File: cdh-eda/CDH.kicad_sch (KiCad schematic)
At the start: 4 parts

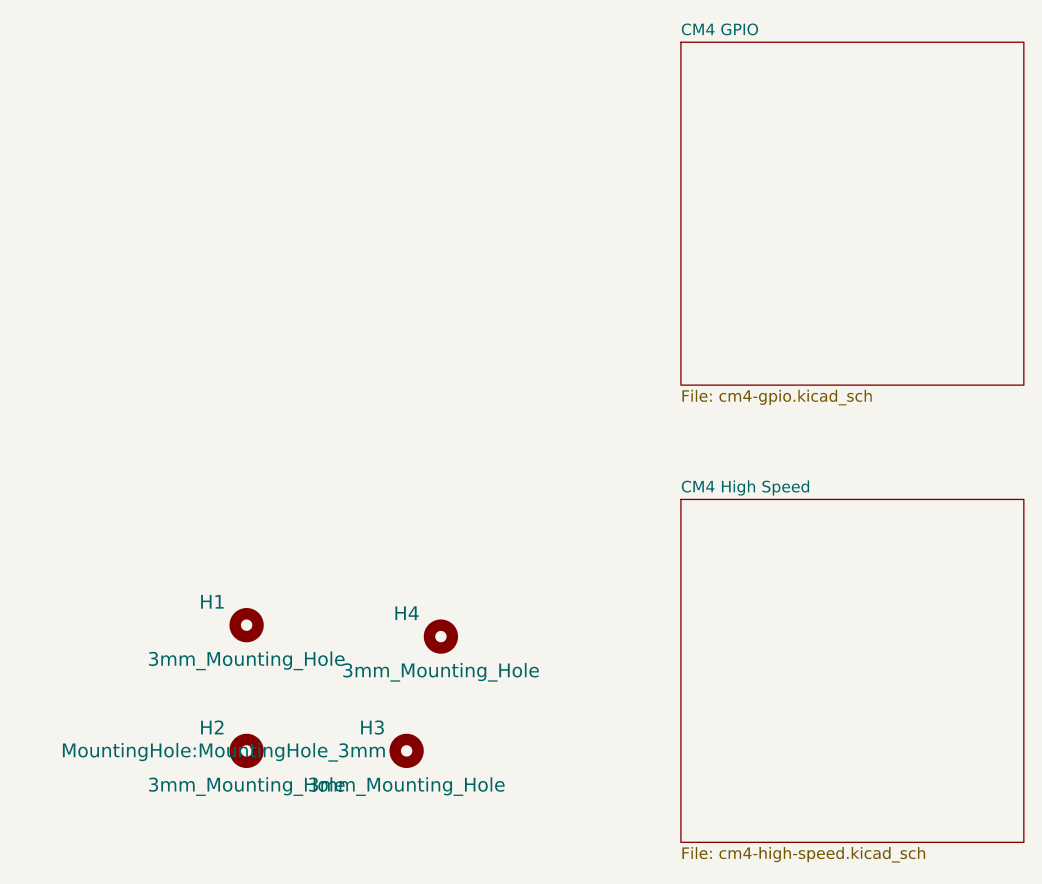
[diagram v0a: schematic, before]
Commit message: V.2 updates
 1. Add jumper CAN resistors
 2. Add camera connector
 3. Add display connector
 5. Updated CAN transceiver protective circuitry
 6. Add MCP2515 interrupt GPIO pin 18
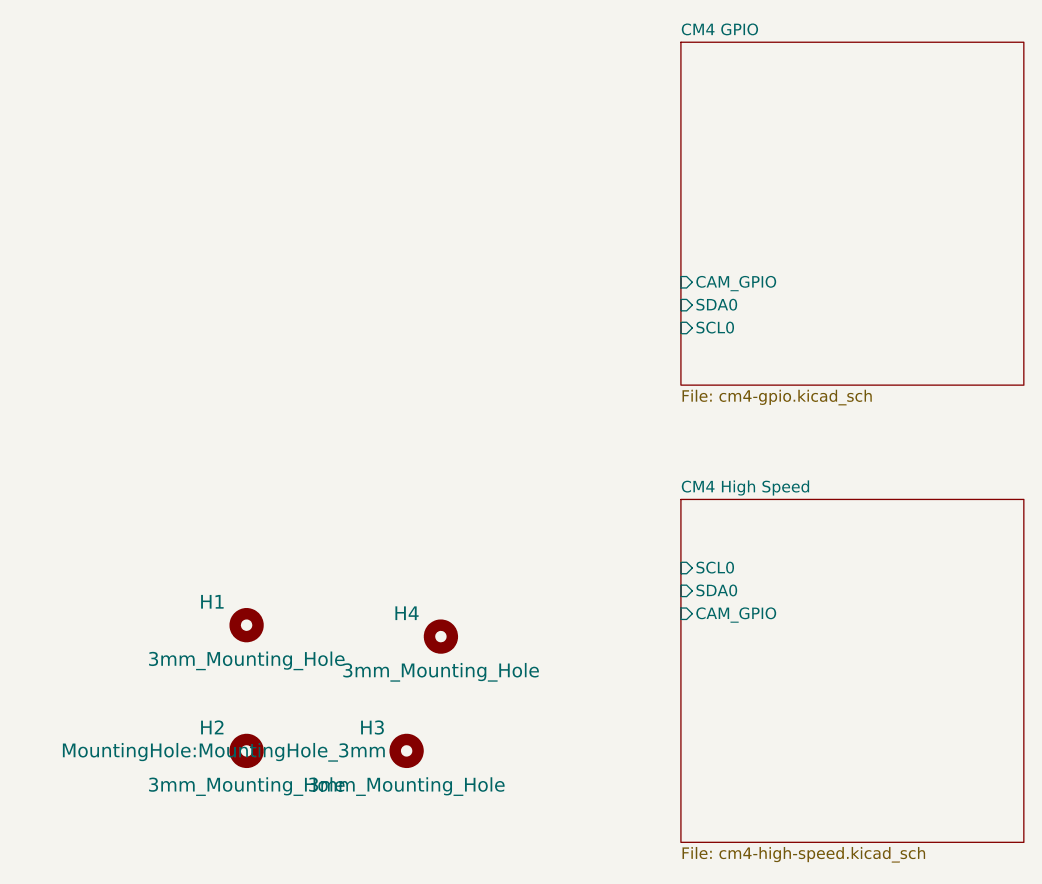
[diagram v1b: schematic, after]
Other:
- sheet CM4 GPIO ports: added CAM_GPIO, SCL0, SDA0; removed none
- sheet CM4 High Speed ports: added CAM_GPIO, SCL0, SDA0; removed none
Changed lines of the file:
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@@
       (effects (font (size 1.27 1.27)) (justify left top))
+    )
+    (pin "SCL0" input (at 101.6 109.22 180)
+      (effects (font (size 1.27 1.27)) (justify left))
+    )
+    (pin "SDA0" input (at 101.6 111.76 180)
+      (effects (font (size 1.27 1.27)) (justify left))
+    )
+    (pin "CAM_GPIO" input (at 101.6 114.3 180)
+      (effects (font (size 1.27 1.27)) (justify left))
     )
   )
@@
       (effects (font (size 1.27 1.27)) (justify left top))
     )
+    (pin "SDA0" input (at 101.6 80.01 180)
+      (effects (font (size 1.27 1.27)) (justify left))
+    )
+    (pin "SCL0" input (at 101.6 82.55 180)
+      (effects (font (size 1.27 1.27)) (justify left))
+    )
+    (pin "CAM_GPIO" input (at 101.6 77.47 180)
+      (effects (font (size 1.27 1.27)) (justify left))
+    )
   )
   (sheet_instances
@@
   )
   (symbol_instances
-    (path "/fc4c71a5-1008-4ac4-98db-57c838c57d91/bdbbddee-eed0-4002-a2d6-91bf5b52af91"
-      (reference "#PWR01") (unit 1) (value "GND") (footprint "")
-    )
     (path "/fc4c71a5-1008-4ac4-98db-57c838c57d91/75d513cd-8ea6-4bff-84e6-f70e2fe56b9c"
       (reference "#PWR0101") (unit 1) (value "GND") (footprint "")
@@
       (reference "#PWR0102") (unit 1) (value "GND") (footprint "")
     )
-    (path "/fc4c71a5-1008-4ac4-98db-57c838c57d91/d3fc070e-eaae-41bc-af26-49ae9801fba8"
+    (path "/fc4c71a5-1008-4ac4-98db-57c838c57d91/31fde201-dc10-4f30-906f-fc313141b188"
       (reference "#PWR0103") (unit 1) (value "GND") (footprint "")
     )
@@
       (reference "#PWR0108") (unit 1) (value "GND") (footprint "")
     )
-    (path "/fc4c71a5-1008-4ac4-98db-57c838c57d91/e4cfdfe4-01e4-43aa-a760-865662d559fe"
+    (path "/caa71f4c-454d-4ac9-b287-456eafb34991/0ad2dbcc-680f-4d79-840c-e8ea7bda806d"
       (reference "#PWR0109") (unit 1) (value "GND") (footprint "")
     )
@@
       (reference "#PWR0117") (unit 1) (value "GND") (footprint "")
     )
+    (path "/caa71f4c-454d-4ac9-b287-456eafb34991/d1878e1d-1a34-432e-b4ba-873c2a461ca3"
+      (reference "#PWR0118") (unit 1) (value "GND") (footprint "")
+    )
+    (path "/fc4c71a5-1008-4ac4-98db-57c838c57d91/e1b93949-2c17-47fa-a708-a0e6d23d85e6"
+      (reference "#PWR0119") (unit 1) (value "GND") (footprint "")
+    )
     (path "/fc4c71a5-1008-4ac4-98db-57c838c57d91/c3d2db6e-c256-429f-9fa3-16b8bad2bd05"
       (reference "C1") (unit 1) (value "10u") (footprint "Capacitor_SMD:C_0603_1608Metric")
@@
       (reference "C2") (unit 1) (value "100n") (footprint "Capacitor_SMD:C_0603_1608Metric")
     )
-    (path "/fc4c71a5-1008-4ac4-98db-57c838c57d91/d012336a-c822-4ad9-b694-344f9e761ddc"
+    (path "/fc4c71a5-1008-4ac4-98db-57c838c57d91/5fb90b6d-dad2-480b-bdcd-9b6852b6311f"
       (reference "C3") (unit 1) (value "100n") (footprint "Capacitor_SMD:C_0603_1608Metric")
+    )
+    (path "/fc4c71a5-1008-4ac4-98db-57c838c57d91/96d117dc-7175-4cad-b6c1-db0ea99834fd"
+      (reference "C4") (unit 1) (value "4.7nF") (footprint "Capacitor_SMD:C_0603_1608Metric")
+    )
+    (path "/caa71f4c-454d-4ac9-b287-456eafb34991/c3156dfe-ad86-452a-942c-d88fa4ce14f4"
+      (reference "Camera1") (unit 1) (value "Conn_01x22_Female") (footprint "Connector_FFC-FPC:Hirose_FH12-22S-0.5SH_1x22-1MP_P0.50mm_Horizontal")
     )
     (path "/fc4c71a5-1008-4ac4-98db-57c838c57d91/a079bbfb-fc64-4018-9e03-8f2993b8a67c"
@@
     (path "/fc4c71a5-1008-4ac4-98db-57c838c57d91/15f875cc-7b84-4cb1-9382-30fb7facf120"
       (reference "D2") (unit 1) (value "LED Red") (footprint "LED_SMD:LED_0603_1608Metric")
+    )
+    (path "/caa71f4c-454d-4ac9-b287-456eafb34991/0464560d-a4ad-4361-8c75-1f71f025a1ea"
+      (reference "Display1") (unit 1) (value "Conn_01x22_Female") (footprint "Connector_FFC-FPC:Hirose_FH12-22S-0.5SH_1x22-1MP_P0.50mm_Horizontal")
     )
     (path "/25e21b76-e342-4a30-932e-18b3dc0e3a56"
@@
       (reference "J4") (unit 1) (value "USB_OTG") (footprint "CM4IO:USB_Micro-B_EDAC_UCON00686")
     )
-    (path "/fc4c71a5-1008-4ac4-98db-57c838c57d91/feb84259-3068-4abe-8882-a305c90fa5a3"
-      (reference "JP1") (unit 1) (value "SolderJumper_2_Open") (footprint "Jumper:SolderJumper-2_P1.3mm_Open_RoundedPad1.0x1.5mm")
+    (path "/fc4c71a5-1008-4ac4-98db-57c838c57d91/fc3a8a4c-19f6-4937-9a2e-7bbf2ea51fef"
+      (reference "JP1") (unit 1) (value "SolderJumper_3_Bridged12") (footprint "Jumper:SolderJumper-3_P1.3mm_Bridged2Bar12_RoundedPad1.0x1.5mm")
+    )
+    (path "/fc4c71a5-1008-4ac4-98db-57c838c57d91/5d2e25f6-3296-4563-80cd-54dae1dc9832"
+      (reference "JP2") (unit 1) (value "SolderJumper_3_Bridged12") (footprint "Jumper:SolderJumper-3_P1.3mm_Bridged2Bar12_RoundedPad1.0x1.5mm")
     )
     (path "/caa71f4c-454d-4ac9-b287-456eafb34991/fafda8be-1326-444e-bcc1-8cb4aded3240"
@@
       (reference "R8") (unit 1) (value "2.2K 1%") (footprint "Resistor_SMD:R_0603_1608Metric_Pad0.98x0.95mm_HandSolder")
     )
+    (path "/fc4c71a5-1008-4ac4-98db-57c838c57d91/243644c2-a5a8-4988-b510-037359b44ade"
+      (reference "R9") (unit 1) (value "60") (footprint "Resistor_SMD:R_0603_1608Metric")
+    )
+    (path "/fc4c71a5-1008-4ac4-98db-57c838c57d91/a8c896d7-4d2d-4f7c-b8ee-2516a5e0c980"
+      (reference "R10") (unit 1) (value "60") (footprint "Resistor_SMD:R_0603_1608Metric")
+    )
     (path "/fc4c71a5-1008-4ac4-98db-57c838c57d91/43eb7900-4113-46d7-8d20-69eed69c0afc"
       (reference "U1") (unit 1) (value "ATA6560-GAQW-VAO") (footprint "Package_SO:SOIC-8-1EP_3.9x4.9mm_P1.27mm_EP2.29x3mm")
@@
     )
     (path "/fc4c71a5-1008-4ac4-98db-57c838c57d91/063c1faa-3e03-4e00-977c-3bc076a91e14"
-      (reference "U3") (unit 1) (value "MCP2510-E/SO") (footprint "Package_SO:SOIC-18W_7.5x11.6mm_P1.27mm")
+      (reference "U3") (unit 1) (value "MCP2515T-I/SO") (footprint "Package_SO:SOIC-18W_7.5x11.6mm_P1.27mm")
     )
     (path "/fc4c71a5-1008-4ac4-98db-57c838c57d91/143293a1-7ec4-406b-8e86-2429660aefcf"
